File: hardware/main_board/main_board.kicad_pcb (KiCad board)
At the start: 4 copper layers, 250 x 50 mm, 111 parts, among them J1 USB_C_Receptacle_USB2.0_16P, J2 UART_DEBUG, J3 BAT1, J4 CTRL, J5 LED_CTRL, J6 HV_OUTPUT, Q1 MMBT3904, Q2 MMBT3904, Q3 FDS2734, SW1 SW_MEC_5G, U1 MPU-6050, U10 AMS1117, U11 LM5155, U12 IP5305T, U2 CP2102N-A02-GQFN28, U3 SRV05-4, U4 DFPlayer_mini, U5 ESP32-S3-WROOM1, U6 DS3231MZ, U7 INA3221, U8 BQ27441DRZR-G1A

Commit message: WIP(hardware): update in-4 display board
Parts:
- removed GND1: GND_TP, TestPoint:TestPoint_Pad_D2.0mm
- removed J4: CTRL, Connector_PinSocket_2.00mm:PinSocket_2x03_P2.00mm_Vertical
- removed J5: LED_CTRL, Connector_PinSocket_2.00mm:PinSocket_2x03_P2.00mm_Vertical
- removed J6: HV_OUTPUT, Connector_PinSocket_2.00mm:PinSocket_2x03_P2.00mm_Vertical
- removed SCL1: SCL_TP, TestPoint:TestPoint_Pad_D2.0mm
- removed SDA1: SDA_TP, TestPoint:TestPoint_Pad_D2.0mm
- added J10: Conn_02x05_Counter_Clockwise, Connector_PinHeader_2.00mm:PinHeader_2x05_P2.00mm_Vertical, F.Cu at (266.4, 108.3)
- added J9: Conn_02x05_Counter_Clockwise, Connector_PinHeader_2.00mm:PinHeader_2x05_P2.00mm_Vertical, F.Cu at (123.1, 86.1)
- C36: value 0.47u/200V -> 10u/400v; footprint Capacitor_SMD:C_1206_3216Metric -> johnson:Cap_THT_D8.0mm_L12mm_Horizontal; moved to F.Cu
- J2: footprint Connector_PinHeader_2.54mm:PinHeader_1x04_P2.54mm_Horizontal -> Connector_PinHeader_2.00mm:PinHeader_1x04_P2.00mm_Horizontal; moved to F.Cu
- R32: value 50k -> 1M; footprint Resistor_SMD:R_0603_1608Metric -> Resistor_SMD:R_0805_2012Metric
- R33: value 300 -> 6k; footprint Resistor_SMD:R_0603_1608Metric -> Resistor_SMD:R_0805_2012Metric
- U4, U8: moved to F.Cu
- moved C7 168.6 mm to (75.3, 48.3), turned to 180 degrees
- moved SW1 133.4 mm to (198.8, 19.4)
- moved R18 125.3 mm to (79.6, 37.1), turned to 180 degrees
- moved D1 119.6 mm to (209.8, 42.5), turned to 180 degrees
- moved D2 116.4 mm to (209.8, 44.5), turned to 180 degrees
- moved C14 116.3 mm to (91.6, 37.1), turned to 180 degrees
- moved U6 116.1 mm to (207.3, 19.5)
- moved R16 114.2 mm to (195.9, 39.6)
- moved D3 113.2 mm to (209.8, 46.5), turned to 180 degrees
- moved C16 112.6 mm to (91.6, 42.1), turned to 180 degrees
- moved R27 112.4 mm to (181.3, 17.4), turned to 180 degrees
- moved R28 110.7 mm to (181.3, 19.9), turned to 180 degrees
- moved D4 110.1 mm to (209.8, 48.5), turned to 180 degrees
- moved C17 109.9 mm to (91.6, 44.6), turned to 180 degrees
- moved R30 108.3 mm to (181.3, 24.9), turned to 180 degrees
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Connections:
- U5 pad 8: RGB_LED_DO -> unconnected-(U5-IO15-Pad8)
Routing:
- net GND: track 437.9 -> 0.00 mm, vias 38 -> 0
- net RGB_LED_DI: track 185.8 -> 0.00 mm, vias 1 -> 0
- net RGB_LED_DO: track 184.9 -> 0.00 mm, vias 1 -> 0
- net +5V: track 171.5 -> 0.00 mm, vias 3 -> 0
- net HV_PWR+: track 164.9 -> 0.00 mm, vias 3 -> 0
- net +3V3: track 162.2 -> 0.00 mm, vias 12 -> 0
- net I2C0_SCL: track 153.7 -> 0.00 mm, vias 4 -> 0
- net I2C0_SDA: track 147.1 -> 0.00 mm, vias 3 -> 0
- net LED_PWR+: track 130.8 -> 0.00 mm, vias 1 -> 0
- net BAT_LOW: track 90.9 -> 0.00 mm, vias 3 -> 0
- net VBUS: track 68.7 -> 0.00 mm, vias 3 -> 0
- net ~{RTC_INT}: track 67.0 -> 0.00 mm, vias 2 -> 0
- net HV_PG: track 66.1 -> 0.00 mm, vias 3 -> 0
- net CHIP_PU: track 55.3 -> 0.00 mm, vias 2 -> 0
- net Net-(U11-FB): track 53.9 -> 0.00 mm
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- removed copper zone on F.Cu, net +3V3
- removed copper zone on F.Cu, net GND
- removed copper zone on In2.Cu, net GND
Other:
- outline, holes or cut-outs redrawn
- board text removed: "+3V3"
- board text removed: "D+"
- board text removed: "D-"
- board text removed: "GND"
- board text removed: "RX"
- board text removed: "SPEAKER"
- board text removed: "TX"

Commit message: WIP(hardware): in4 display board layout
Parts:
- removed J10, J9: Conn_02x05_Counter_Clockwise, Connector_PinHeader_2.00mm:PinHeader_2x05_P2.00mm_Vertical
- added J4: Conn_02x05_Odd_Even, Connector_PinHeader_2.00mm:PinHeader_2x05_P2.00mm_Vertical, F.Cu at (178.2, 107.0)
- added J5: Conn_02x05_Odd_Even, Connector_PinHeader_2.00mm:PinHeader_2x05_P2.00mm_Vertical, F.Cu at (112.2, 141.0)
- moved U8 185.6 mm to (262.1, -8.68)
- moved LS1 151.0 mm to (105.0, 115.5), turned to 0 degrees
- moved U4 145.3 mm to (90.5, 103.7)
- moved U5 136.0 mm to (46.9, 121.1), turned to -90 degrees
- moved Q3 134.7 mm to (122.3, 34.7)
- moved J3 94.6 mm to (208.5, 141.5), turned to 90 degrees
- moved J2 88.7 mm to (57.5, 104.0)
- moved H3 72.1 mm to (218.0, 141.0)
- moved C36 62.3 mm to (195.9, 102.0), turned to -90 degrees
- moved H4 51.9 mm to (218.0, 101.0)
- moved H1 48.5 mm to (74.0, 141.0)
- moved H2 47.1 mm to (74.0, 101.0)
- moved U10 25.0 mm to (120.0, 69.5)
- moved U12 23.9 mm to (134.3, 59.1)
- moved J1 17.3 mm to (146.0, 139.0)
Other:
- board size 250 x 50 mm -> 230 x 50 mm

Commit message: WIP(hardware): update main board and mainboard layout
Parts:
- removed R3, R4: 10k, Resistor_SMD:R_0603_1608Metric
- added C38: 2.2u/35V, Capacitor_SMD:C_0805_2012Metric, B.Cu at (161.4, 108.2)
- added C39: 22u/10V, Capacitor_SMD:C_1206_3216Metric, B.Cu at (154.2, 113.6)
- added C40: 100n, Capacitor_SMD:C_0402_1005Metric, B.Cu at (152.9, 115.4)
- added C41: 1u, Capacitor_SMD:C_0603_1608Metric, B.Cu at (164.8, 112.6)
- added C42: 0.1u, Capacitor_SMD:C_0603_1608Metric, B.Cu at (166.6, 112.6)
- added C43: 0.1u, Capacitor_SMD:C_0603_1608Metric, B.Cu at (97.2, 121.5)
- added JP7: NC, Jumper:SolderJumper-2_P1.3mm_Bridged_RoundedPad1.0x1.5mm, B.Cu at (160.9, 113.8)
- added JP8: NO, Jumper:SolderJumper-2_P1.3mm_Open_RoundedPad1.0x1.5mm, B.Cu at (142.8, 118.5)
- added L3: 10uH, Inductor_SMD:L_Changjiang_FNR4010S, B.Cu at (154.0, 108.8)
- added Q10: MMBTA42, Package_TO_SOT_SMD:SOT-23, B.Cu at (205.8, 101.0)
- added Q11: MMBTA92, Package_TO_SOT_SMD:SOT-23, B.Cu at (201.0, 100.6)
- added Q12: MMBTA42, Package_TO_SOT_SMD:SOT-23, B.Cu at (196.7, 101.1)
- added Q13: MMBTA92, Package_TO_SOT_SMD:SOT-23, B.Cu at (191.9, 100.7)
- added Q14: MMBTA42, Package_TO_SOT_SMD:SOT-23, B.Cu at (180.8, 113.9)
- added Q15: MMBTA92, Package_TO_SOT_SMD:SOT-23, B.Cu at (185.6, 114.3)
- added Q4: MMBTA92, Package_TO_SOT_SMD:SOT-23, B.Cu at (171.3, 110.8)
- added Q5: MMBTA42, Package_TO_SOT_SMD:SOT-23, B.Cu at (176.0, 111.1)
- added Q6: MMBTA42, Package_TO_SOT_SMD:SOT-23, B.Cu at (168.0, 102.8)
- added Q7: MMBTA92, Package_TO_SOT_SMD:SOT-23, B.Cu at (172.7, 103.1)
- added Q8: MMBTA42, Package_TO_SOT_SMD:SOT-23, B.Cu at (177.0, 98.6)
- added Q9: MMBTA92, Package_TO_SOT_SMD:SOT-23, B.Cu at (182.3, 100.8)
- added R19: 100k, Resistor_SMD:R_0402_1005Metric, B.Cu at (157.4, 111.7)
- added R21: 1M, Resistor_SMD:R_0603_1608Metric, B.Cu at (173.0, 113.0)
- added R34: 470k, Resistor_SMD:R_0603_1608Metric, B.Cu at (173.8, 109.2)
- added R35: 47k, Resistor_SMD:R_0603_1608Metric, B.Cu at (170.6, 113.5)
- added R36: 10k, Resistor_SMD:R_0603_1608Metric, B.Cu at (175.6, 114.0)
- added R37: 10k, Resistor_SMD:R_0603_1608Metric, B.Cu at (168.0, 99.8)
- added R38: 470k, Resistor_SMD:R_0603_1608Metric, B.Cu at (170.2, 104.6)
- added R39: 1M, Resistor_SMD:R_0603_1608Metric, B.Cu at (171.0, 101.0)
- added R40: 47k, Resistor_SMD:R_0603_1608Metric, B.Cu at (173.4, 100.6)
- added R41: 10k, Resistor_SMD:R_0603_1608Metric, B.Cu at (177.0, 101.6)
- added R42: 470k, Resistor_SMD:R_0603_1608Metric, B.Cu at (180.9, 98.2)
- added R43: 1M, Resistor_SMD:R_0603_1608Metric, B.Cu at (184.4, 99.0)
- added R44: 47k, Resistor_SMD:R_0603_1608Metric, B.Cu at (185.1, 101.4)
- added R45: 10k, Resistor_SMD:R_0603_1608Metric, B.Cu at (205.8, 103.8)
- added R46: 470k, Resistor_SMD:R_0603_1608Metric, B.Cu at (203.6, 99.2)
- added R47: 1M, Resistor_SMD:R_0603_1608Metric, B.Cu at (202.8, 102.8)
- added R48: 47k, Resistor_SMD:R_0603_1608Metric, B.Cu at (200.4, 103.2)
- added R49: 10k, Resistor_SMD:R_0603_1608Metric, B.Cu at (196.7, 103.9)
- added R50: 470k, Resistor_SMD:R_0603_1608Metric, B.Cu at (194.5, 99.3)
- added R51: 1M, Resistor_SMD:R_0603_1608Metric, B.Cu at (193.7, 102.9)
- added R52: 47k, Resistor_SMD:R_0603_1608Metric, B.Cu at (191.3, 103.3)
- added R53: 10k, Resistor_SMD:R_0603_1608Metric, B.Cu at (180.8, 111.0)
- added R54: 470k, Resistor_SMD:R_0603_1608Metric, B.Cu at (183.1, 115.7)
- added R55: 1M, Resistor_SMD:R_0603_1608Metric, B.Cu at (183.8, 112.0)
- added R56: 47k, Resistor_SMD:R_0603_1608Metric, B.Cu at (186.2, 111.8)
- added U13: 74HC238, Package_DFN_QFN:DHVQFN-16-1EP_2.5x3.5mm_P0.5mm_EP1x2mm, B.Cu at (166.8, 108.5)
- added U9: TPS62177DQC, Package_SON:WSON-10-1EP_2x3mm_P0.5mm_EP0.84x2.4mm_ThermalVias, B.Cu at (158.3, 109.1)
- C36, J2, U4, U8: moved to B.Cu
- moved R17 166.9 mm to (208.0, 141.1), turned to -90 degrees
- moved R20 165.2 mm to (210.0, 141.0), turned to -90 degrees
- moved C19 161.9 mm to (208.0, 137.8), turned to -90 degrees
- moved U8 158.0 mm to (205.2, 138.7), turned to -90 degrees
- moved C13 157.0 mm to (210.0, 137.7), turned to -90 degrees
- moved U6 154.1 mm to (95.2, 125.2)
- moved R15 146.6 mm to (183.2, 135.7), turned to 90 degrees
- moved C11 137.8 mm to (183.2, 132.5), turned to 90 degrees
- moved C10 137.4 mm to (177.4, 134.4)
- moved U1 137.3 mm to (106.2, 126.2)
- moved SW1 128.1 mm to (160.2, 141.6)
- moved C25 126.8 mm to (159.7, 118.8), turned to 90 degrees
- moved C26 126.7 mm to (156.0, 118.9)
- moved R32 125.9 mm to (157.0, 132.9), turned to 90 degrees
- moved R9 125.9 mm to (165.0, 140.6), turned to -90 degrees
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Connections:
- net ANODE renamed /hv_power/PWR_HV+
- C21 pad 1: +5V -> Net-(JP8-B)
- C22 pad 1: +5V -> Net-(JP8-B)
- J4 pad 10: ANODE5 -> /nixie_anode_mux/T4_E
- J4 pad 2: ANODE1 -> /nixie_anode_mux/T0_E
- J4 pad 4: ANODE2 -> /nixie_anode_mux/T1_E
- J4 pad 6: ANODE3 -> /nixie_anode_mux/T2_E
- J4 pad 8: ANODE4 -> /nixie_anode_mux/T3_E
- J4 pad 9: ANODE6 -> /nixie_anode_mux/T5_E
- U10 pad 3: +5V -> Net-(JP8-B)
- U5 pad 10: U1TXD -> unconnected-(U5-IO17-Pad10)
- U5 pad 11: U1RXD -> unconnected-(U5-IO18-Pad11)
- U5 pad 12: ~{RTC_INT} -> unconnected-(U5-IO8-Pad12)
- U5 pad 17: unconnected-(U5-IO9-Pad17) -> /nixie_anode_mux/T0
- U5 pad 18: unconnected-(U5-IO10-Pad18) -> /nixie_anode_mux/T1
- U5 pad 19: unconnected-(U5-IO11-Pad19) -> /nixie_anode_mux/T2
- U5 pad 34: unconnected-(U5-IO41-Pad34) -> U1TXD
- U5 pad 35: unconnected-(U5-IO42-Pad35) -> U1RXD
- U5 pad 38: unconnected-(U5-IO2-Pad38) -> ~{RTC_INT}
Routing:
- net GND: track 0.00 -> 329.7 mm, vias 0 -> 23
- net I2C0_SDA: track 0.00 -> 202.9 mm, vias 0 -> 4
- net I2C0_SCL: track 0.00 -> 194.1 mm, vias 0 -> 3
- net +3V3: track 0.00 -> 179.7 mm, vias 0 -> 18
- net VBAT: track 0.00 -> 149.4 mm, vias 0 -> 3
- net +5V: track 0.00 -> 147.7 mm, vias 0 -> 8
- net /hv_power/PWR_HV+: track 0.00 -> 116.8 mm, vias 0 -> 7
- net BAT_LOW: track 0.00 -> 105.9 mm, vias 0 -> 3
- net VBUS: track 0.00 -> 68.9 mm, vias 0 -> 5
- net USB_D-: track 0.00 -> 53.9 mm, vias 0 -> 2
- net Net-(J2-Pin_2): track 0.00 -> 52.2 mm, vias 0 -> 2
- net USB_D+: track 0.00 -> 51.6 mm, vias 0 -> 2
- net ~{NIXIE_OE}: track 0.00 -> 50.9 mm, vias 0 -> 2
- net Net-(J2-Pin_3): track 0.00 -> 48.0 mm, vias 0 -> 2
- net RGB_LED_DI: track 0.00 -> 45.8 mm, vias 0 -> 2
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- added copper zone on B.Cu, net +3V3
- added copper zone on F.Cu, net +3V3
- added copper zone on F.Cu, net GND
- added copper zone on In2.Cu, net GND
- added copper zone on B.Cu, net HV_PWR+
- added copper zone on B.Cu, net Net-(D6-A)
- added copper zone on In1.Cu, net Net-(D6-A)
- added copper zone on In2.Cu, net Net-(D6-A)
- added copper zone on B.Cu, net Net-(U9-SW)
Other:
- outline, holes or cut-outs redrawn
- board text added: "+170VDC"
- board text added: "+3V3"
- board text added: "170VDC"
- board text added: "4.2V Lipo battery only"
- board text added: "BAT+"
- board text added: "BRDGE_D+"
- board text added: "BRDGE_D-"
- board text added: "BUCK3V3"
- board text added: "ESP32_D+"
- board text added: "ESP32_D-"
- board text added: "GND"
- board text added: "LDO3V3"
- board text added: "LED_PWR+"
- board text added: "NC"
- board text added: "NIXIE_OE"
- board text added: "Nixie Clock V1.9.0 ESP32_MAIN_BOARD"
- board text added: "RGBLED_DI"
- board text added: "RXD"
- board text added: "SCL"
- board text added: "SDA"
- board text added: "T0_E"
- board text added: "T1_E"
- board text added: "T2_E"
- board text added: "T3_E"
- board text added: "T4_E"
- board text added: "T5_E"
- board text added: "TXD"

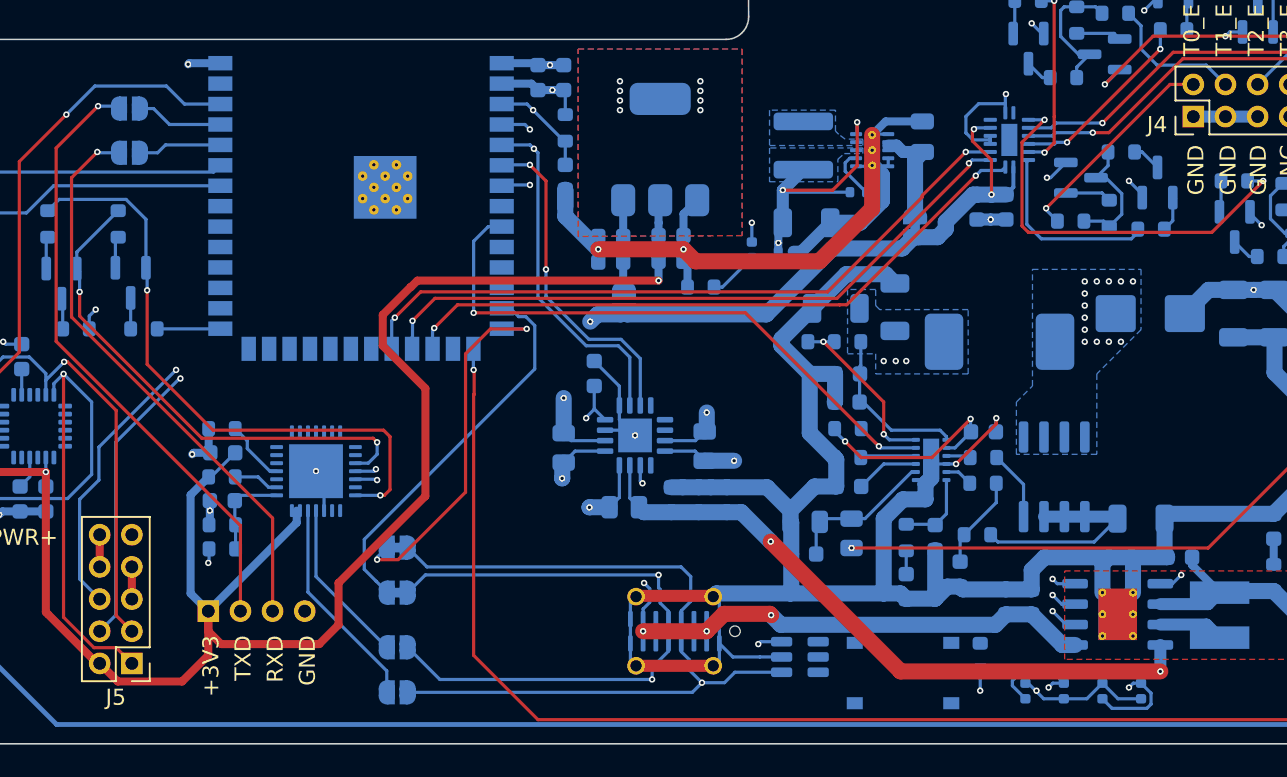
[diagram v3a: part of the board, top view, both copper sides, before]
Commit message: chore(hardware): complete mainboard layout
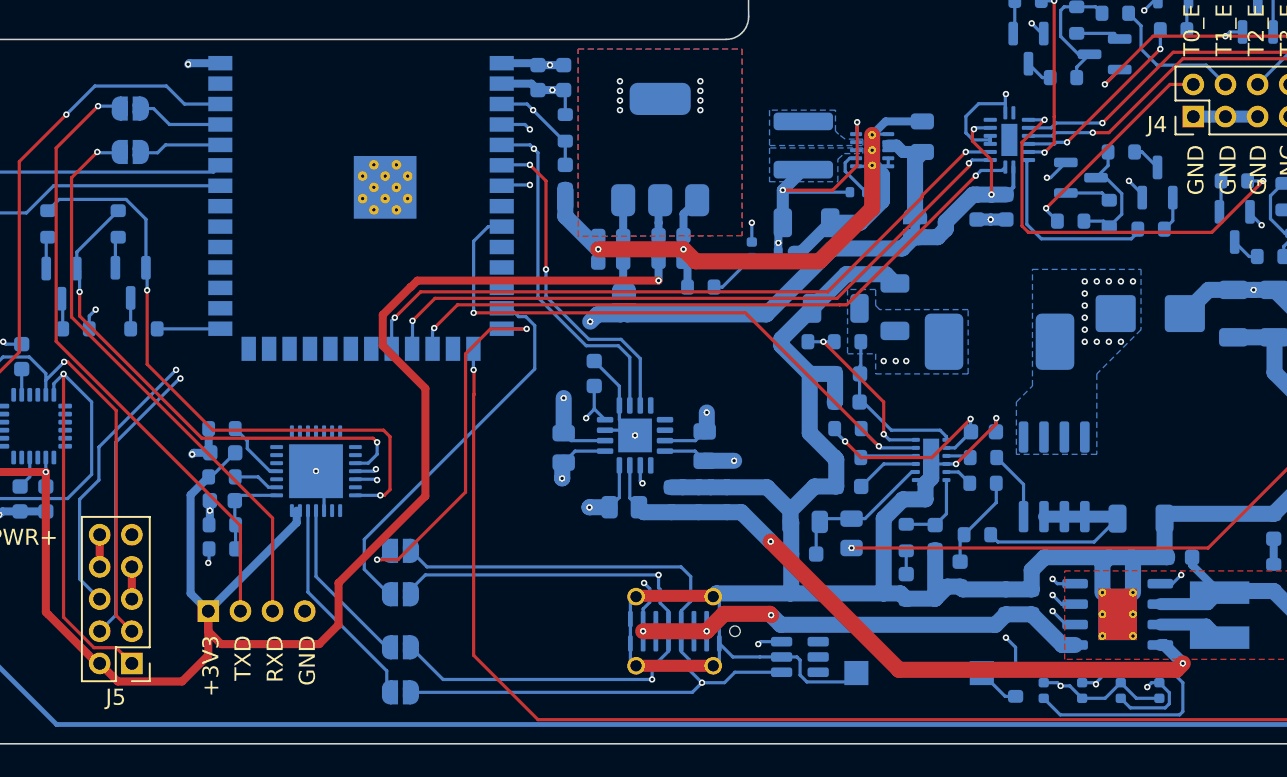
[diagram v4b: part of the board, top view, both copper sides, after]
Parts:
- added G***: LOGO, johnson:HR_logo_10mmx10mm, B.Cu at (94.0, 136.8)
- JP1, JP2, JP3, JP4: value NO -> NC
- JP5, JP6: value NC -> NO; footprint Jumper:SolderJumper-2_P1.3mm_Bridged_RoundedPad1.0x1.5mm -> Jumper:SolderJumper-2_P1.3mm_Open_RoundedPad1.0x1.5mm
- SW1: value SW_MEC_5G -> SW_Push; footprint Button_Switch_SMD:SW_Push_1P1T_XKB_TS-1187A -> Button_Switch_SMD:SW_SPST_CK_RS282G05A3
- moved R9 2.75 mm to (167.2, 142.2), turned to 90 degrees
- moved D1 1.14 mm to (168.9, 142.7)
- moved D2 1.14 mm to (171.3, 142.7)
- moved D3 1.14 mm to (173.7, 142.7)
- moved D4 1.14 mm to (176.1, 142.7)
- moved SW1 1.00 mm to (161.2, 141.6)
- moved JP6 0.28 mm to (128.9, 134.0)
- moved JP5 0.22 mm to (128.9, 136.7)
- moved JP1 0.20 mm to (128.9, 142.8)
- moved JP2 0.20 mm to (128.9, 140.0)
- moved JP3 0.07 mm to (112.2, 109.2)
- moved JP4 0.05 mm to (112.2, 106.5)
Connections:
- SW1 pad 2: Net-(R9-Pad1) -> GND
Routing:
- net Net-(D1-A): track 12.7 -> 25.6 mm
- net GND: track 329.7 -> 335.7 mm
- net Net-(U12-KEY): track 20.4 -> 17.4 mm
- net Net-(R9-Pad1): track 0.00 -> 2.70 mm
- net +5V_CHG: track 41.1 -> 42.9 mm
- net Net-(D3-A): track 15.2 -> 16.9 mm
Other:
- board text added: "3w/8Ω"
- board text added: "Nixie Clock V1.9.0 MAIN_BOARD"
- board text added: "RXD0"
- board text added: "TXD0"
- board text removed: "Nixie Clock V1.9.0 ESP32_MAIN_BOARD"

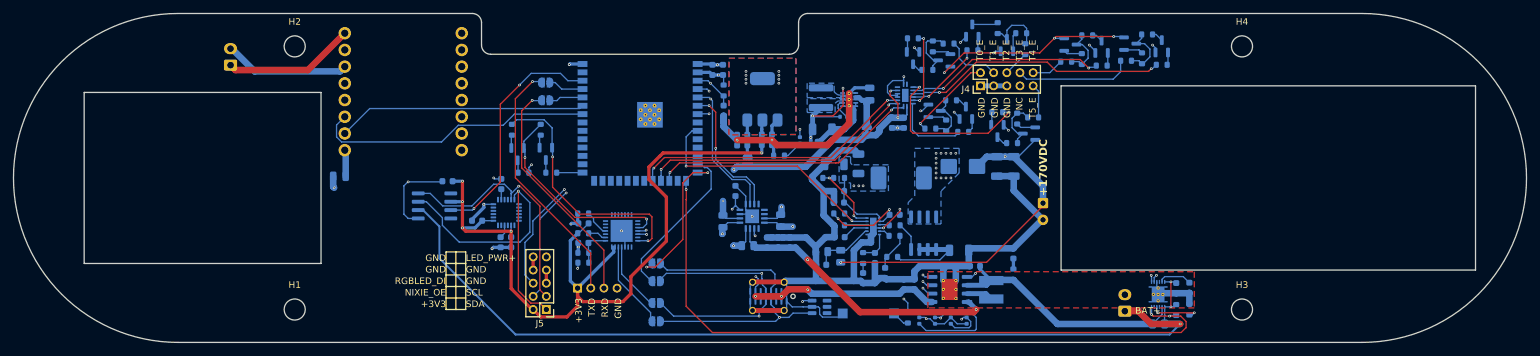
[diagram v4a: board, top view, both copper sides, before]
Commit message: chore(hardware): shrink main board size to lower the PCB price
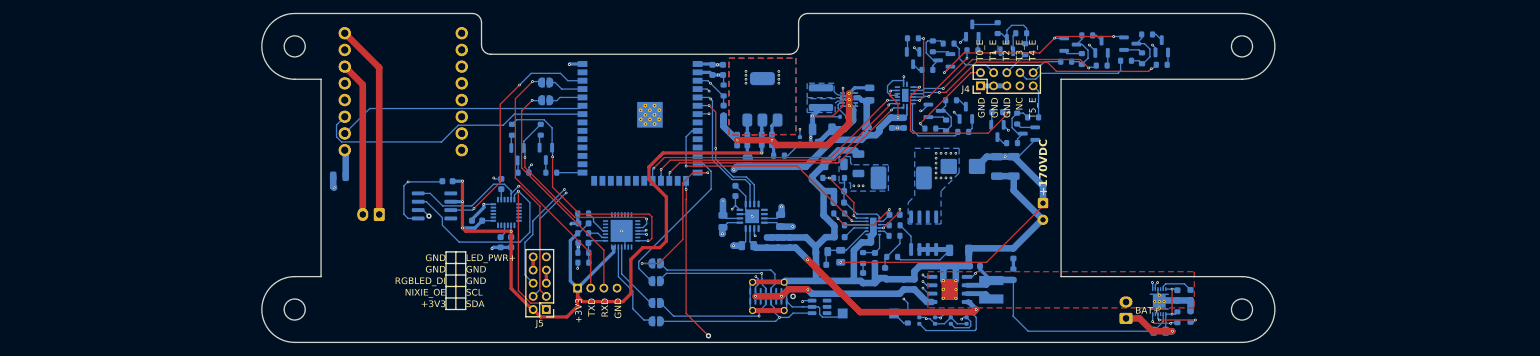
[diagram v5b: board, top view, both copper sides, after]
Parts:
- moved LS1 32.0 mm to (86.8, 126.6), turned to 180 degrees
- moved G*** 4.11 mm to (97.6, 134.9)
- moved C13 1.11 mm to (210.2, 138.8)
- moved R16 1.11 mm to (205.5, 144.3)
- moved R17 1.11 mm to (208.2, 142.2)
- moved U8 1.11 mm to (205.4, 139.8)
- moved C19 1.11 mm to (208.2, 138.8)
- moved J3 1.11 mm to (200.4, 142.3)
- moved R20 1.11 mm to (210.2, 142.1)
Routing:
- net VBAT: track 149.4 -> 135.5 mm, vias 3 -> 4
- net Net-(U4-SPK_2): track 20.0 -> 29.7 mm
- net BAT_LOW: track 105.9 -> 98.5 mm, vias 3 -> 4
- net Net-(U4-SPK_1): track 19.1 -> 23.6 mm
- net Net-(U12-BAT): track 37.6 -> 41.5 mm
- net +3V3: track 179.7 -> 181.2 mm
- net Net-(JP6-B): track 23.0 -> 24.2 mm
- net Net-(JP1-B): track 13.4 -> 14.0 mm
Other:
- board size 230 x 50 mm -> 154 x 50 mm
- board text added: "Nixie Clock V1.9.0"
- board text removed: "4.2V Lipo battery only"
- board text removed: "Nixie Clock V1.9.0 MAIN_BOARD"

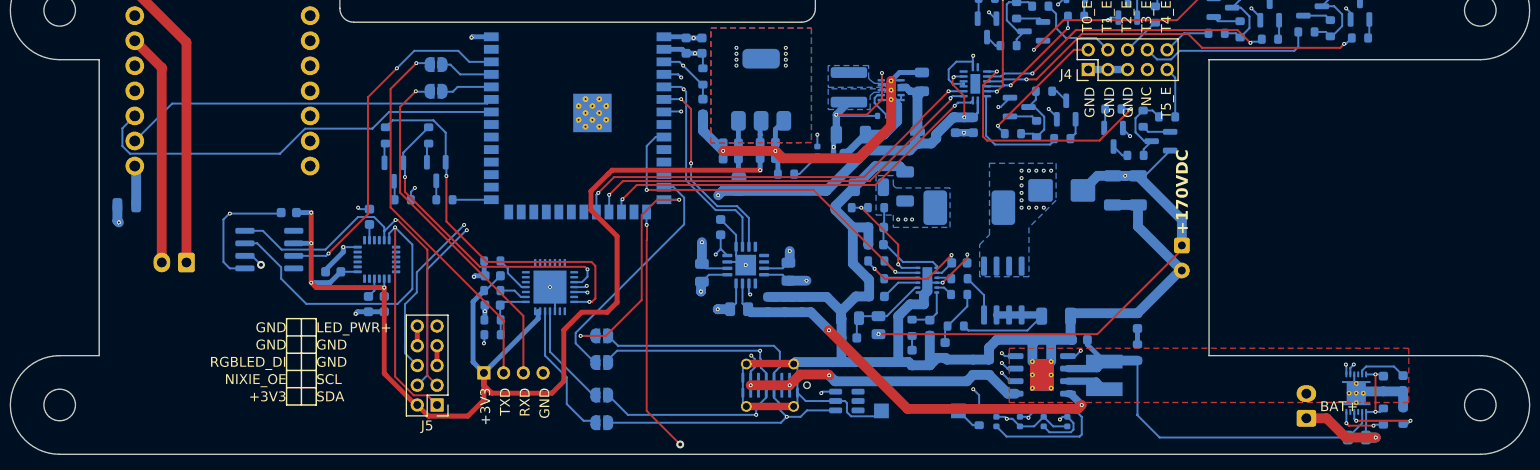
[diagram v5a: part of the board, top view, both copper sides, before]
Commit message: chore(hardware): update bom and LCSC SN
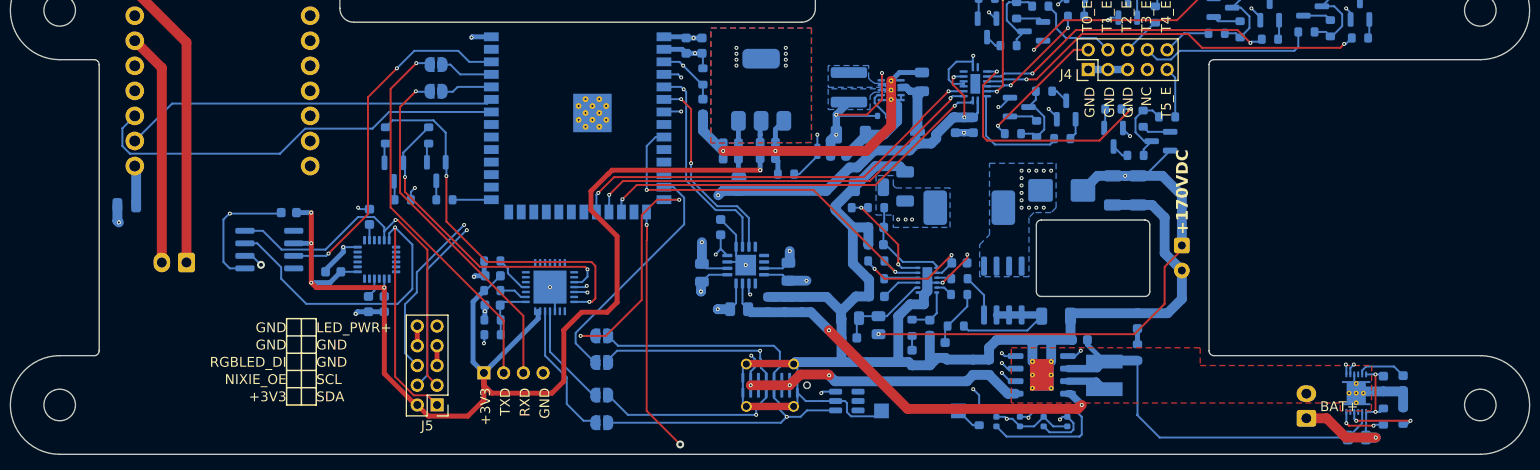
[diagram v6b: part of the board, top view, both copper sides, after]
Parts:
- C39: value 22u/10V -> 22u
- C40: value 100n -> 0.1u; footprint Capacitor_SMD:C_0402_1005Metric -> Capacitor_SMD:C_0603_1608Metric
- moved C40 0.35 mm to (152.9, 115.8)
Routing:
- net /hv_power/PWR_HV+: track 116.8 -> 120.4 mm
- net +3V3: track 181.2 -> 183.2 mm
- net GND: track 335.7 -> 337.6 mm
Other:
- outline, holes or cut-outs redrawn
